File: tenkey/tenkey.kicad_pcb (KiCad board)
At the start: 2 copper layers, 39 parts, among them SW0:0 NUM_0, SW0:2 DOT, SW1:0 NUM_1, SW1:1 NUM_2, SW1:2 NUM_3, SW1:3 ENTER, SW2:0 NUM_4, SW2:1 NUM_5, SW2:2 NUM_6, SW3:0 NUM_7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

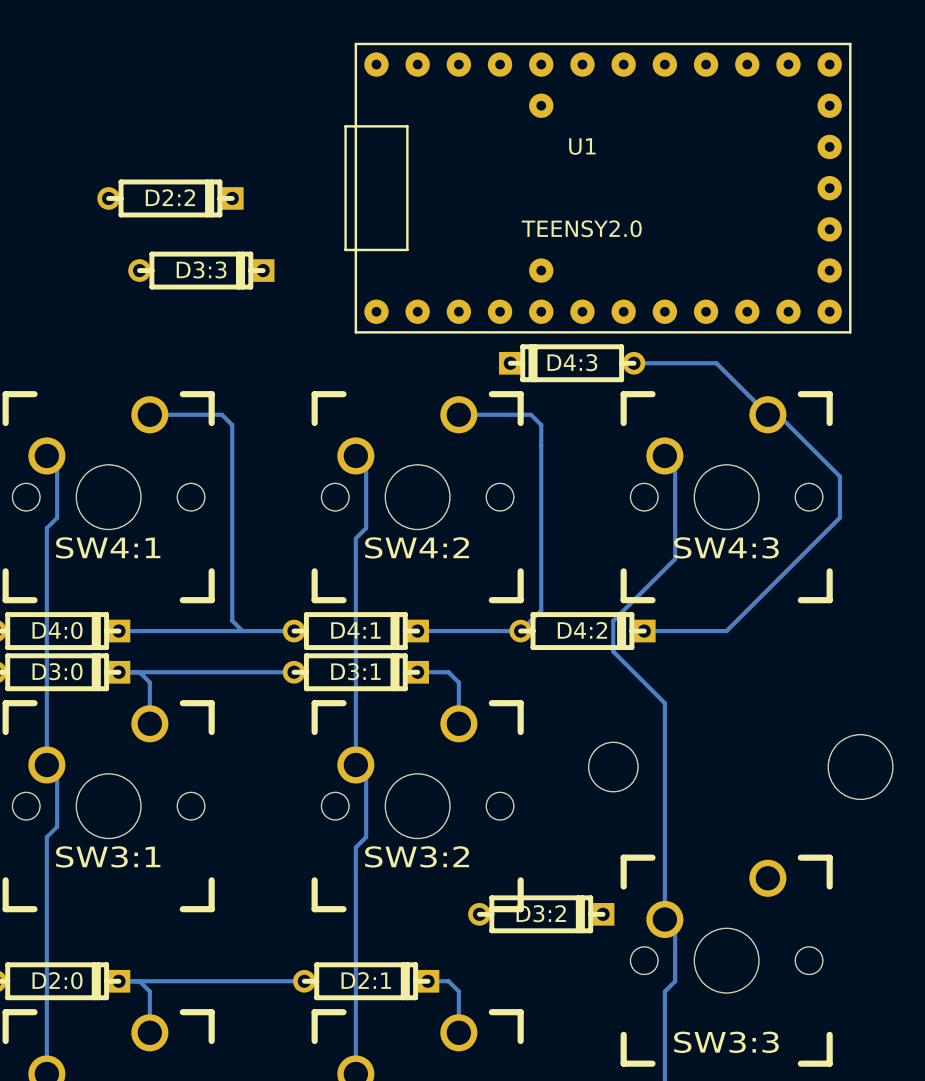
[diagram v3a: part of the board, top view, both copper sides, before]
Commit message: tenkey routed except for row/cols to teensy
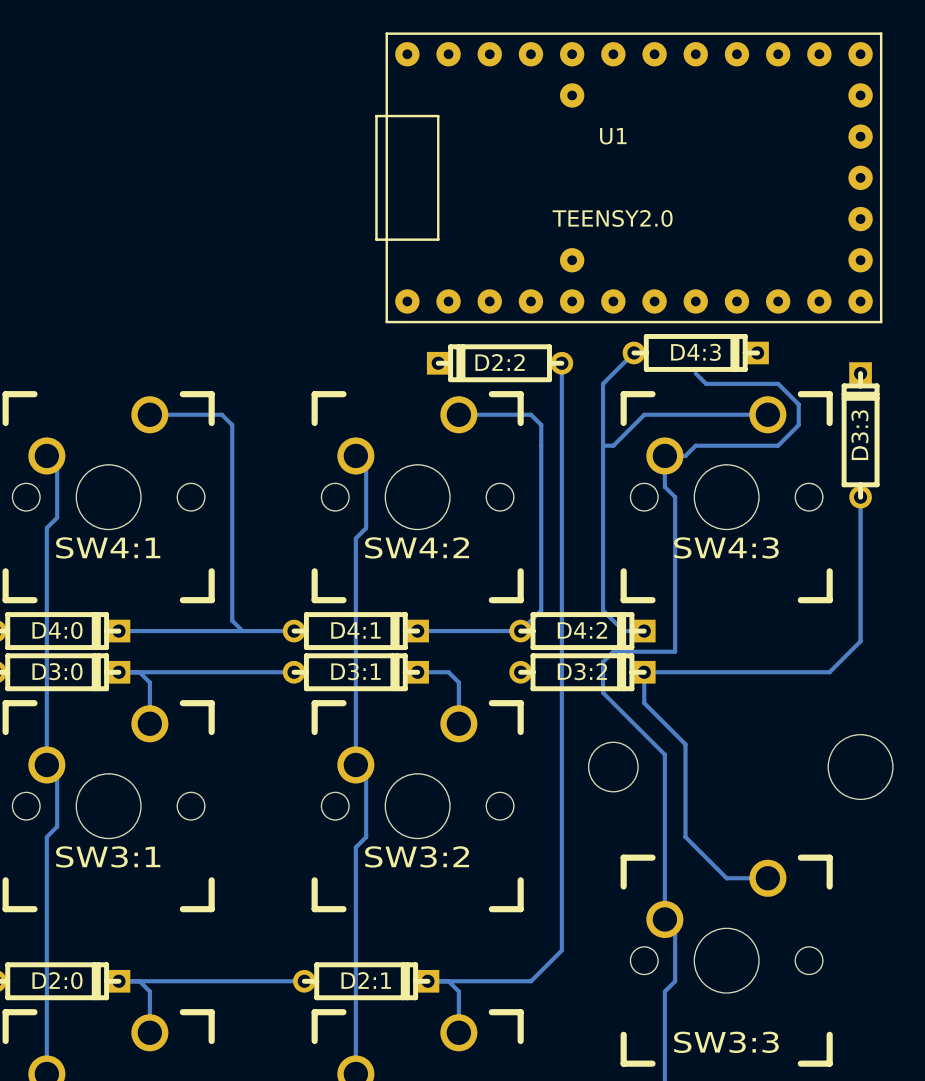
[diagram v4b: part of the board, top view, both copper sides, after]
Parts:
- moved D3:3 41.9 mm to (176.5, 73.0), turned to 90 degrees
- moved D2:2 22.7 mm to (154.3, 68.6), turned to 180 degrees
- moved D3:2 15.1 mm to (159.4, 87.6)
- moved D4:3 7.65 mm to (166.4, 67.9), turned to 0 degrees
- moved U1 2.01 mm to (161.3, 57.1)
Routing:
- net Net-(D2:1-Pad2): track 4.71 -> 49.9 mm
- net Net-(D3:2-Pad2): track 0.00 -> 40.4 mm
- net /COL3: track 71.3 -> 92.4 mm
- net Net-(D4:2-Pad2): track 33.1 -> 31.9 mm

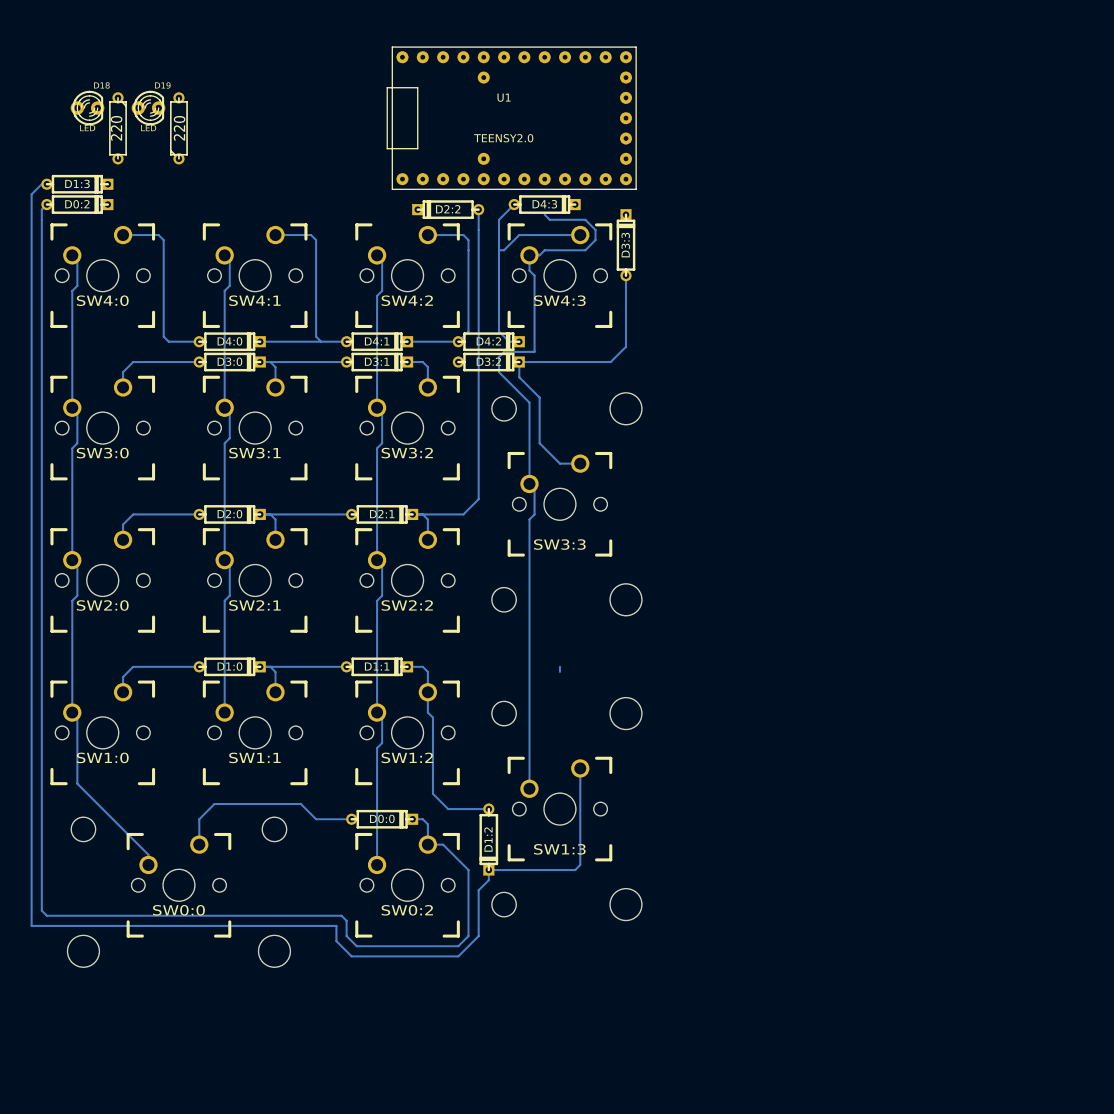
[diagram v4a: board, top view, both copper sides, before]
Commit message: tenkey finished pcb routing and adjusting pinout
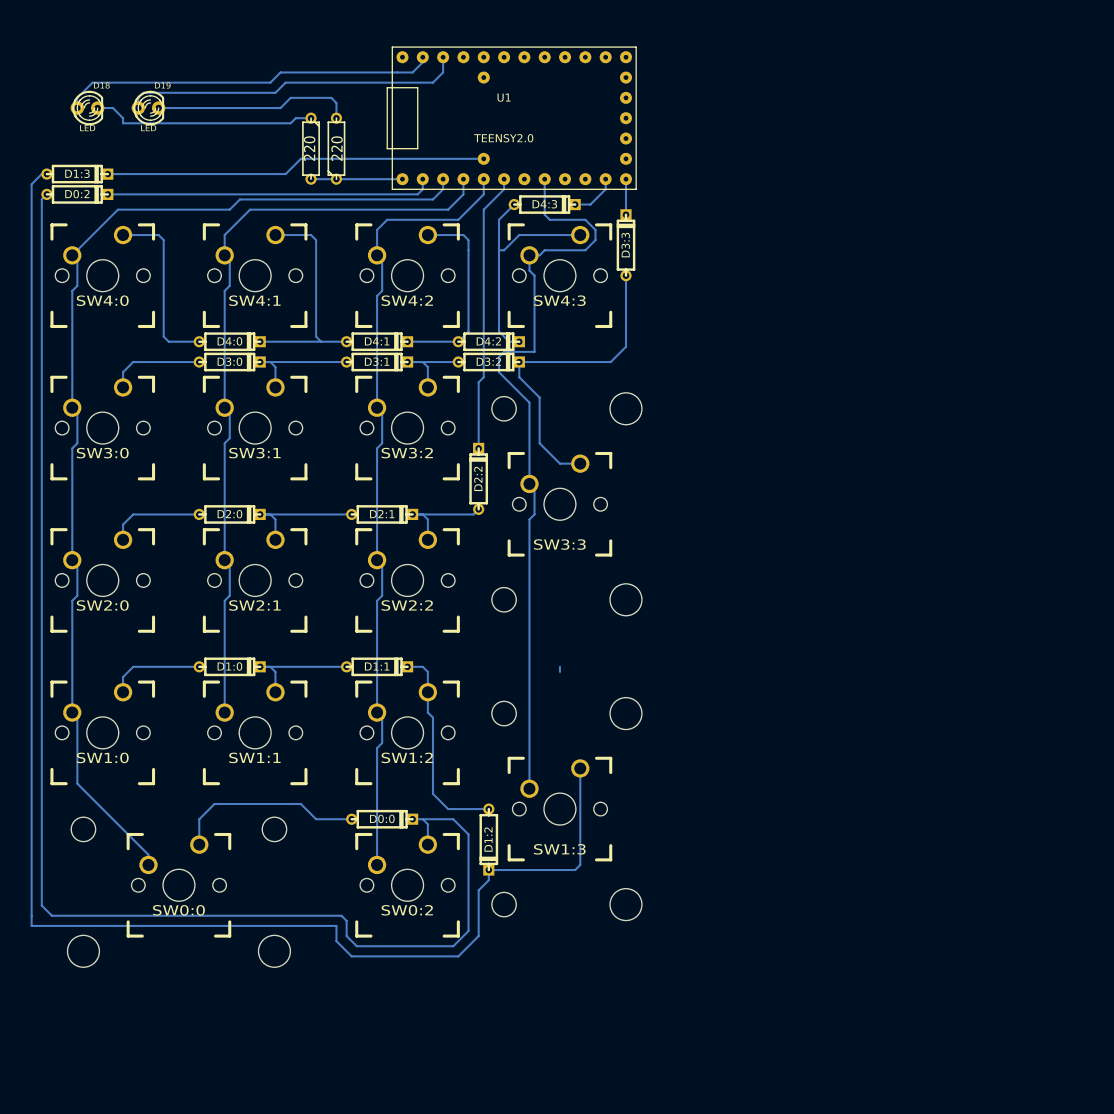
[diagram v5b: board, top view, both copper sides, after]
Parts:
- moved D2:2 33.9 mm to (158.1, 102.2), turned to 90 degrees
- moved R1 24.3 mm to (137.2, 61.0)
- moved R2 19.8 mm to (140.3, 61.0)
- moved D0:2 1.27 mm to (108.0, 66.7)
- moved D1:3 1.27 mm to (108.0, 64.1)
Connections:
- R2 pad 1: Net-(R2-Pad1) -> Net-(R1-Pad2)
- U1 pad 1: /ROW1 -> /COL0
- U1 pad 10: Net-(U1-Pad10) -> /ROW3
- U1 pad 11: /COL1 -> Net-(U1-Pad11)
- U1 pad 12: /COL2 -> Net-(U1-Pad12)
- U1 pad 13: /COL3 -> Net-(U1-Pad13)
- U1 pad 14: /LED_A -> Net-(U1-Pad14)
- U1 pad 15: /LED_B -> Net-(U1-Pad15)
- U1 pad 2: /ROW2 -> /COL1
- U1 pad 20: Net-(U1-Pad20) -> /LED_B
- U1 pad 21: Net-(U1-Pad21) -> /LED_A
- U1 pad 22: /COL0 -> Net-(U1-Pad22)
- U1 pad 24: Net-(U1-Pad24) -> /ROW1
- U1 pad 27: VCC -> Net-(U1-Pad27)
- U1 pad 28: VCC -> Net-(U1-Pad28)
- U1 pad 3: /ROW3 -> /COL2
- U1 pad 30: Net-(U1-Pad30) -> Net-(R1-Pad2)
- U1 pad 4: Net-(U1-Pad4) -> /ROW2
- U1 pad 6: Net-(U1-Pad6) -> /COL3
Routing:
- net /COL0: track 81.7 -> 132.8 mm
- net /ROW1: track 0.00 -> 47.8 mm
- net /LED_A: track 0.00 -> 46.9 mm
- net /LED_B: track 0.00 -> 42.6 mm
- net /ROW0: track 0.00 -> 40.9 mm
- net Net-(D2:1-Pad2): track 49.9 -> 13.2 mm
- net /COL1: track 58.7 -> 95.1 mm
- net /ROW2: track 0.00 -> 35.0 mm
- net Net-(D18-Pad2): track 0.00 -> 28.1 mm
- net Net-(D19-Pad2): track 0.00 -> 24.9 mm
- net /COL2: track 78.3 -> 98.6 mm
- net Net-(R1-Pad2): track 0.00 -> 11.4 mm
- net Net-(D3:1-Pad2): track 5.34 -> 11.7 mm
- net /ROW4: track 0.00 -> 5.87 mm
- net Net-(D0:0-Pad2): track 164.7 -> 169.8 mm
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
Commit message: teensie is gone, were building this with the straight ATMega32u4
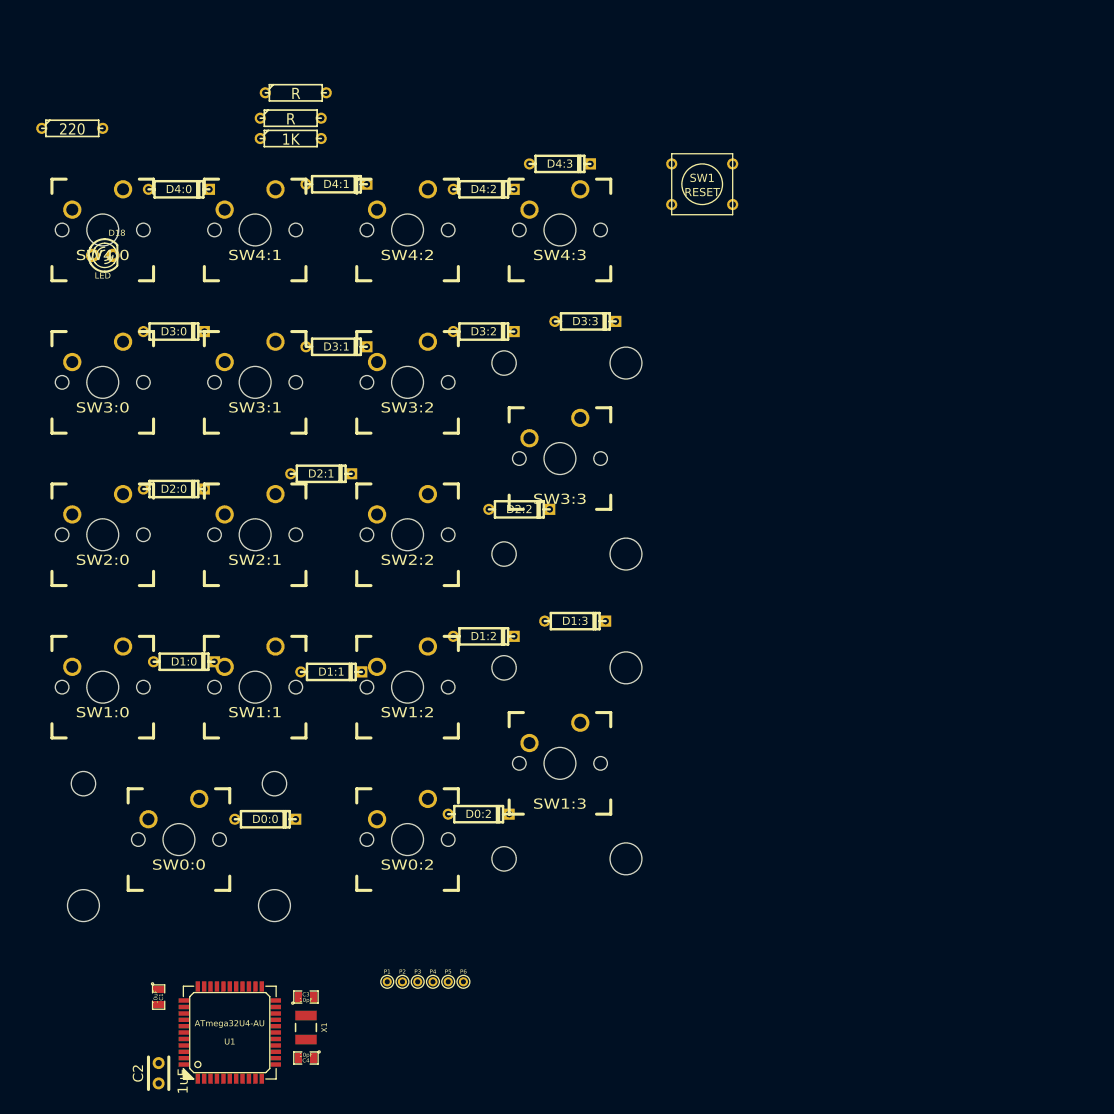
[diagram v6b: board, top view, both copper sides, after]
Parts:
- removed D19: LED, LEDs:LED-3MM
- removed R2: 220, Discret:R3
- added C1: 10uF, SMD_Packages:SM0805, F.Cu at (118.1, 167.0)
- added C2: 1uF, Capacitors_ThroughHole:Capacitor4x3RM2.5, F.Cu at (118.1, 177.8)
- added C3: 10pF, SMD_Packages:SM0805, F.Cu at (136.5, 167.0)
- added C4: 10pF, SMD_Packages:SM0805, F.Cu at (136.5, 174.6)
- added P1: SCK, Connect:PINTST, F.Cu at (146.7, 165.1)
- added P2: MISO, Connect:PINTST, F.Cu at (148.6, 165.1)
- added P3: MOSI, Connect:PINTST, F.Cu at (150.5, 165.1)
- added P4: RESET, Connect:PINTST, F.Cu at (152.4, 165.1)
- added P5: 5V, Connect:PINTST, F.Cu at (154.3, 165.1)
- added P6: GND, Connect:PINTST, F.Cu at (156.2, 165.1)
- added R3: R, Discret:R3, F.Cu at (135.3, 54.0)
- added R4: R, Discret:R3, F.Cu at (134.6, 57.1)
- added R5: 1K, Discret:R3, F.Cu at (134.6, 59.7)
- added SW1: RESET, Discret:SW_PUSH_SMALL, F.Cu at (186.1, 65.4)
- added X1: CRYSTAL, Keyboard:SMD-3225, F.Cu at (136.5, 170.8)
- SW0:2, SW1:0, SW1:1, SW1:2, SW2:0, SW2:1, SW2:2, SW3:0, SW3:1, SW3:2, SW4:0, SW4:1, SW4:2, SW4:3: footprint 1u:CHERRY_PCB_100H -> Keyboard:CHERRY_PCB_100H
- U1: value TEENSY2.0 -> ATmega32U4-AU; footprint Keyboard:TEENSY2_0 -> QFP:lqfp44
- moved U1 119.3 mm to (127.0, 171.4)
- moved D0:2 92.3 mm to (158.1, 144.1)
- moved D1:3 83.6 mm to (170.2, 120.0)
- moved R1 30.0 mm to (107.3, 58.4), turned to 0 degrees
- moved D1:2 25.4 mm to (158.8, 121.9), turned to 0 degrees
- moved D4:1 20.3 mm to (140.3, 65.4)
- moved D4:0 20.1 mm to (120.7, 66.0)
- moved D4:2 19.1 mm to (158.8, 66.0)
- moved D18 18.5 mm to (111.1, 74.3)
- moved D0:0 14.6 mm to (131.4, 144.8)
- moved D3:3 10.8 mm to (171.4, 82.5), turned to 0 degrees
- moved D2:1 9.16 mm to (138.4, 101.6)
- moved D3:0 7.96 mm to (120.0, 83.8)
- moved D2:0 7.67 mm to (120.0, 103.5)
- moved D2:2 6.35 mm to (163.2, 106.0), turned to 0 degrees
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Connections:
- R1 pad 2: Net-(R1-Pad2) -> GND
- U1 pad 1: /COL0 -> Net-(U1-Pad1)
- U1 pad 10: /ROW3 -> /MOSI
- U1 pad 11: Net-(U1-Pad11) -> /MISO
- U1 pad 13: Net-(U1-Pad13) -> /RESET
- U1 pad 14: Net-(U1-Pad14) -> /+5V
- U1 pad 15: Net-(U1-Pad15) -> GND
- U1 pad 2: /COL1 -> /+5V
- U1 pad 20: /LED_B -> Net-(U1-Pad20)
- U1 pad 21: /LED_A -> Net-(U1-Pad21)
- U1 pad 23: Net-(U1-Pad23) -> GND
- U1 pad 24: /ROW1 -> /+5V
- U1 pad 3: /COL2 -> Net-(R3-Pad1)
- U1 pad 30: Net-(R1-Pad2) -> Net-(U1-Pad30)
- U1 pad 4: /ROW2 -> Net-(R4-Pad1)
- U1 pad 5: Net-(U1-Pad5) -> GND
- U1 pad 6: /COL3 -> Net-(C2-Pad1)
- U1 pad 7: Net-(U1-Pad7) -> /+5V
- U1 pad 9: /ROW4 -> /SCK
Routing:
- net Net-(D1:2-Pad2): track 187.3 -> 0.00 mm
- net Net-(D0:0-Pad2): track 169.8 -> 0.00 mm
- net /COL0: track 132.8 -> 0.00 mm
- net /COL2: track 98.6 -> 0.00 mm
- net /COL3: track 96.8 -> 0.00 mm
- net /COL1: track 95.1 -> 0.00 mm
- net /ROW1: track 47.8 -> 0.00 mm
- net /LED_A: track 46.9 -> 0.00 mm
- net /LED_B: track 42.6 -> 0.00 mm
- net /ROW0: track 40.9 -> 0.00 mm
- net Net-(D3:2-Pad2): track 40.4 -> 0.00 mm
- net /ROW2: track 35.0 -> 0.00 mm
- net Net-(D4:2-Pad2): track 31.9 -> 0.00 mm
- net Net-(D4:0-Pad2): track 29.1 -> 0.00 mm
- net Net-(D18-Pad2): track 28.1 -> 0.00 mm
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
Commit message: changed some footprints to SMD
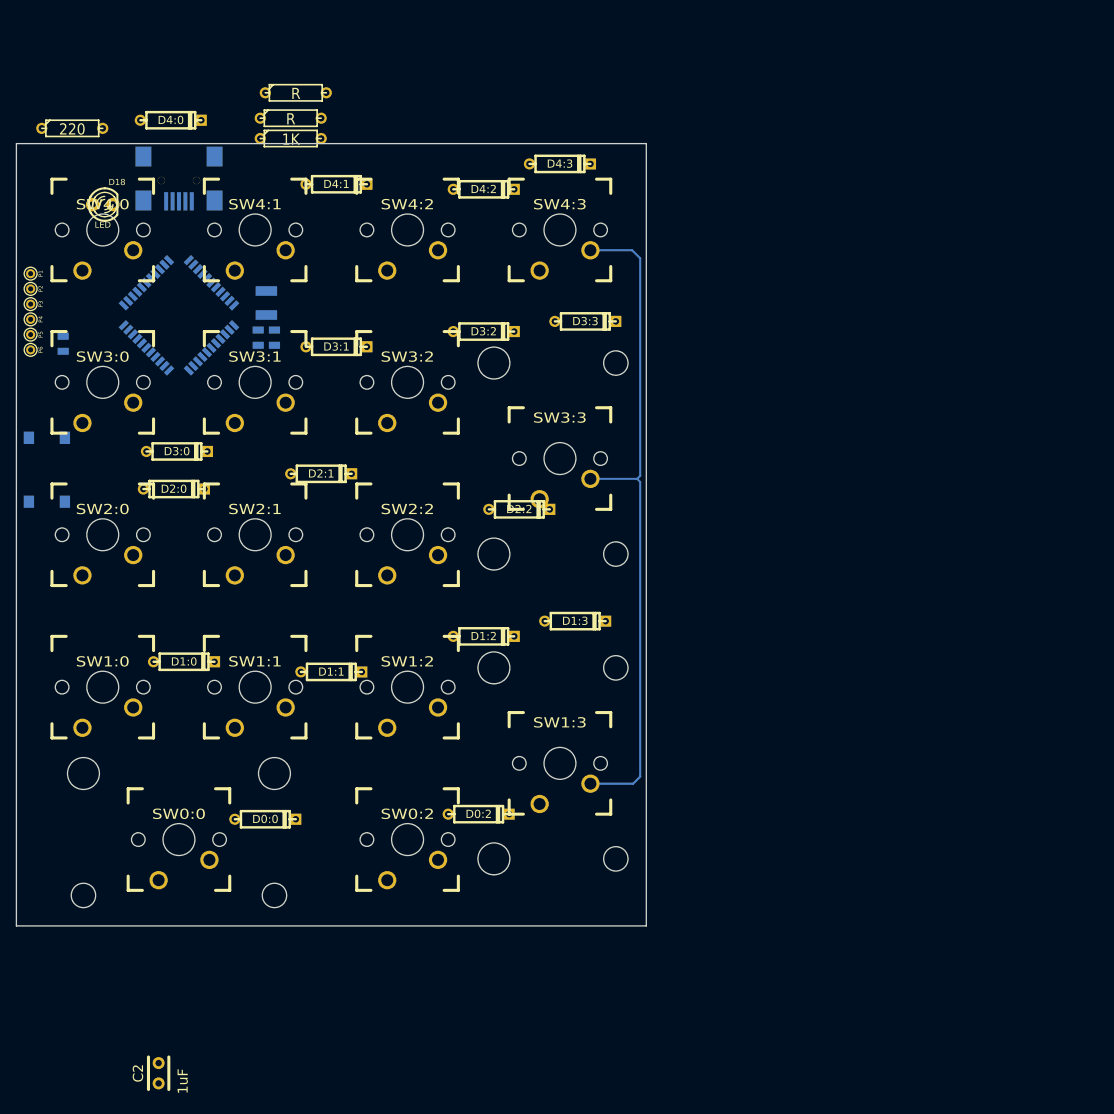
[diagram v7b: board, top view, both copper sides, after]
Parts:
- added J1: USB, Keyboard:USB-MINI-B-SMD, B.Cu at (120.7, 59.7)
- C1, C3, C4, U1, X1: moved to B.Cu
- SW1: footprint Discret:SW_PUSH_SMALL -> Keyboard:SW_PUSH_SMD; moved to B.Cu
- moved P1 99.1 mm to (102.1, 76.6), turned to 270 degrees
- moved P2 98.3 mm to (102.1, 78.5), turned to 270 degrees
- moved P3 97.6 mm to (102.1, 80.4), turned to 270 degrees
- moved P4 96.9 mm to (102.1, 82.3), turned to 270 degrees
- moved P5 96.3 mm to (102.1, 84.2), turned to 270 degrees
- moved P6 95.7 mm to (102.1, 86.1), turned to 270 degrees
- moved X1 90.7 mm to (131.6, 80.3)
- moved C4 90.1 mm to (132.6, 84.6), turned to 270 degrees
- moved U1 89.9 mm to (120.7, 81.8), turned to 135 degrees
- moved SW1 89.4 mm to (104.1, 101.1), turned to 90 degrees
- moved C3 82.6 mm to (130.6, 84.6), turned to 270 degrees
- moved C1 82.5 mm to (106.2, 85.3)
- moved D3:0 15.0 mm to (120.4, 98.8)
- moved D4:0 8.70 mm to (119.6, 57.4)
- moved D18 6.35 mm to (111.1, 67.9)
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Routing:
- net /COL3: track 0.00 -> 84.2 mm
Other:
- board outline added: 78.7 x 97.8 mm
